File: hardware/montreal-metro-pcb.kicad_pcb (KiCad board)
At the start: 2 copper layers, 160 x 160 mm, 95 parts, among them SW1 TS-1187A-B-A-B, SW2 TS-1187A-B-A-B, SW3 TS-1187A-B-A-B, SW4 TS-1187A-B-A-B, U1 XIAO-RP2040-DIP

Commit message: Official names, hand-pass label defaults, and an unrouted board
- labels: restore the official hyphenated names in the six hand-typed
  labels, keeping the hand-chosen line breaks
- auto_label: defaults now follow the hand pass - beside the station and
  level with it, right before left, nudged only as far as needed, one side
  per run, above / below alternating on level runs, leaders last
- board: every track and via removed; routing will be done by hand.
  Artwork regenerated from the frozen labels (water cut back under them)
- rebuild_board.sh no longer routes unless given --autoroute;
  autoroute.py gains "clear"

DRC: no violations, 0 schematic parity issues, 167 unconnected items
(nothing is routed).

Co-Authored-By: Claude Opus 5.5 <noreply@anthropic.com>
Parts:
- moved ROW5 6.00 mm to (83.2, 81.3)
- moved ROW1 4.24 mm to (140.8, 19.2), turned to 90 degrees
- moved ROW3 2.97 mm to (20.2, 74.7), turned to 0 degrees
- moved ROW2 1.39 mm to (62.2, 47.4), turned to 0 degrees
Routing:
- net +5V: track 740.2 -> 0.00 mm, vias 21 -> 0
- net GND: track 262.2 -> 0.00 mm, vias 32 -> 0
- net LED_OUT: track 97.1 -> 0.00 mm, vias 3 -> 0
- net LED_IN: track 73.3 -> 0.00 mm, vias 1 -> 0
- net Net-(LED64-DO): track 55.1 -> 0.00 mm, vias 2 -> 0
- net Net-(LED31-DO): track 53.3 -> 0.00 mm, vias 2 -> 0
- net BUTTON_02: track 38.9 -> 0.00 mm, vias 2 -> 0
- net BUTTON_04: track 28.8 -> 0.00 mm, vias 2 -> 0
- net Net-(LED15-DO): track 27.2 -> 0.00 mm, vias 2 -> 0
- net BUTTON_01: track 26.1 -> 0.00 mm, vias 2 -> 0
- net Net-(LED2-DO): track 24.1 -> 0.00 mm, vias 2 -> 0
- net ROW6: track 19.1 -> 0.00 mm, vias 2 -> 0
- net BUTTON_03: track 16.6 -> 0.00 mm
- net Net-(LED1-DO): track 13.5 -> 0.00 mm, vias 2 -> 0
- net Net-(LED67-DO): track 12.5 -> 0.00 mm, vias 2 -> 0
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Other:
- board text added: "Champ-de- Mars"
- board text added: "Henri-Bourassa"
- board text added: "Honoré-Beaugrand"
- board text added: "Jean-Talon"
- board text added: "Lucien-L'Allier"
- board text added: "Mont-Royal"
- board text added: "Place- d'Armes"
- board text removed: "Champ-de Mars"
- board text removed: "Henri Bourassa"
- board text removed: "Honoré Beaugrand"
- board text removed: "Jean Talon"
- board text removed: "Lucien L'Allier"
- board text removed: "Mont Royal"
- board text removed: "Place d'Armes"

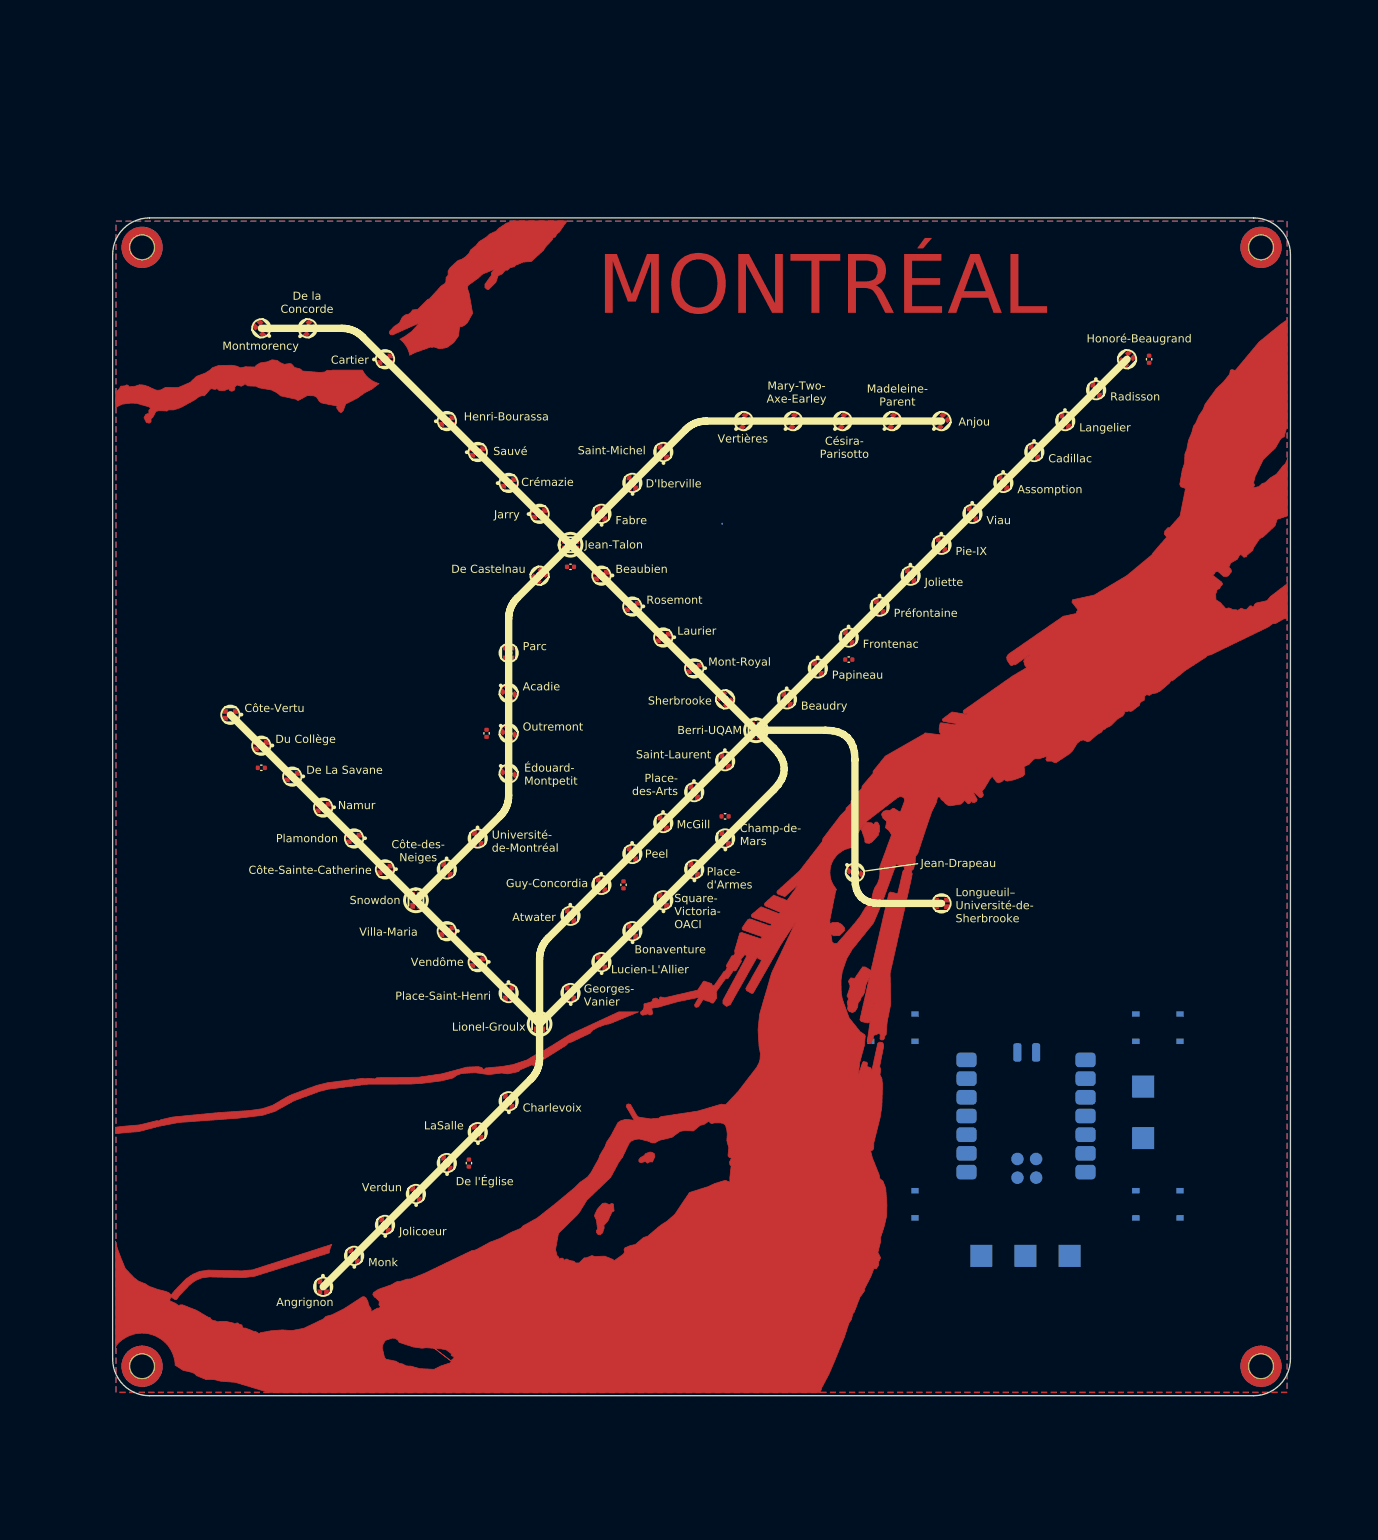
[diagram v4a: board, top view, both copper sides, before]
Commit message: Hand-routed board, R1 and C1, owl back art, JLCPCB outputs
The board is now routed by hand with every assembled part on the
top side. Added:

- C1, 100 uF 6.3 V 1206 X5R bulk capacitor (LCSC C15008, basic)
  on the +5V trunk.
- R1, 330 R 0402 (LCSC C25104, basic) in series on the LED data
  line. U1 pin 8 and the LED_IN1 test point are now on LED_DATA;
  LED_IN runs from R1 to LED1 only.
- The snowy-owl artwork on the back silkscreen as the board-only
  footprint LOGO1, generated by the new tools/svg_to_silk.py.
- JLCPCB gerbers, BOM and CPL in hardware/jlcpcb, stamped
  2026-10-18-1117; make_jlcpcb.py takes the stamp as an argument.
- The latest hand label edits, imported and frozen.

DRC: no errors, 0 unconnected, 0 schematic parity issues.

Co-Authored-By: Claude Opus 5.5 <noreply@anthropic.com>
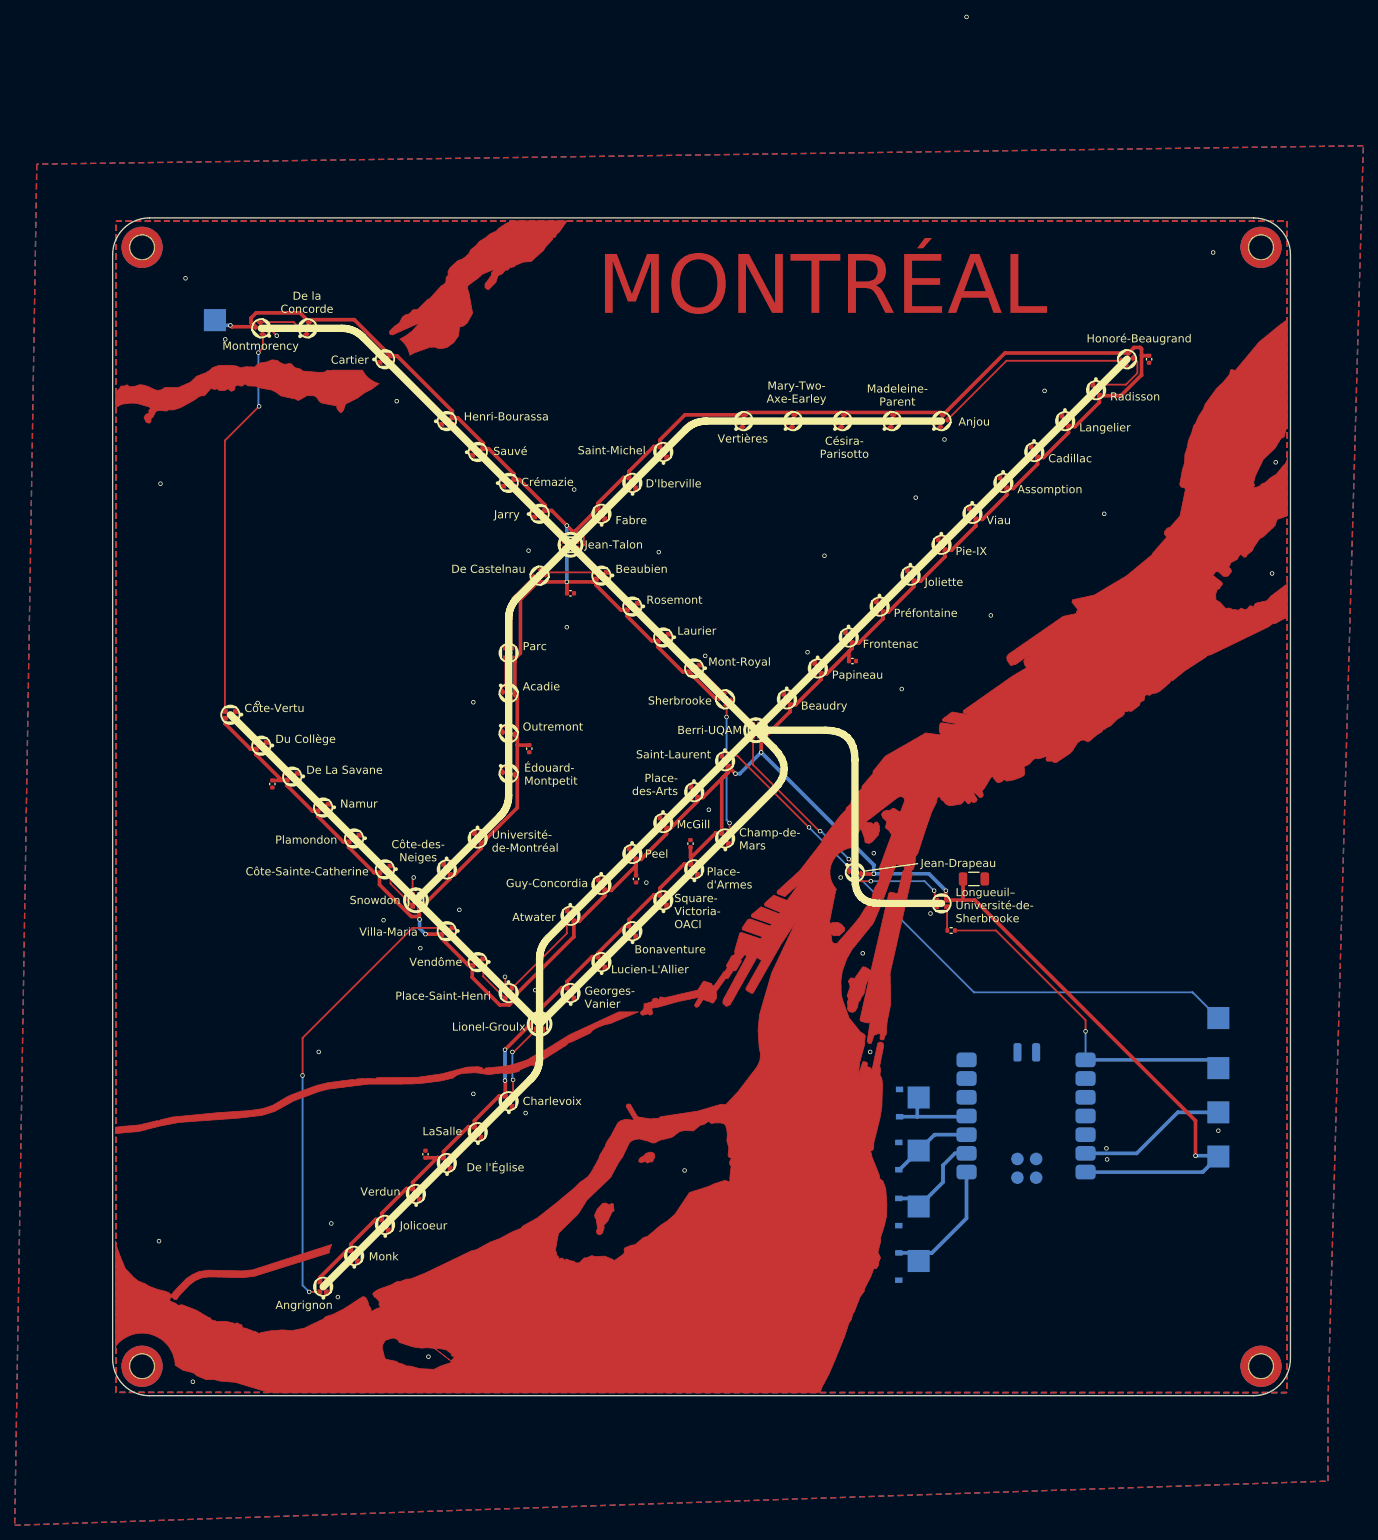
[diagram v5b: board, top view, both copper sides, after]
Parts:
- added C1: 100uF,6.3V,X5R, Capacitor_SMD:C_1206_3216Metric, F.Cu at (117.0, 89.8)
- added LOGO1: artwork, , B.Cu at (80.0, 54.5)
- added R1: 330R, Resistor_SMD:R_0402_1005Metric, F.Cu at (113.9, 96.8)
- added TP1: TestPoint, TestPoint:TestPoint_Pad_3.0x3.0mm, B.Cu at (109.5, 141.7)
- added TP2: TestPoint, TestPoint:TestPoint_Pad_3.0x3.0mm, B.Cu at (109.5, 134.3)
- added TP3: TestPoint, TestPoint:TestPoint_Pad_3.0x3.0mm, B.Cu at (109.5, 126.7)
- added TP4: TestPoint, TestPoint:TestPoint_Pad_3.0x3.0mm, B.Cu at (109.5, 119.5)
- moved +5V1 163.5 mm to (13.9, 13.9), turned to 180 degrees
- moved SW2 42.0 mm to (103.8, 127.5), turned to 0 degrees
- moved LED_IN1 41.1 mm to (150.2, 115.5), turned to -90 degrees
- moved SW4 40.5 mm to (103.9, 120.2), turned to 0 degrees
- moved GND1 32.7 mm to (150.2, 121.5), turned to -90 degrees
- moved SW1 32.5 mm to (103.8, 142.4)
- moved +5V2 24.3 mm to (150.2, 127.5), turned to -90 degrees
- moved LED_OUT1 19.2 mm to (150.2, 108.7)
- moved ROW4 6.16 mm to (56.6, 72.1)
- moved ROW6 6.02 mm to (42.5, 127.2), turned to -90 degrees
- moved ROW5 5.98 mm to (78.5, 85.0), turned to -90 degrees
- moved ROW2 3.60 mm to (62.2, 51.0), turned to 180 degrees
- moved ROW3 2.66 mm to (21.7, 76.9), turned to 90 degrees
- moved SW3 2.44 mm to (103.8, 135.1)
- moved ROW7 1.88 mm to (71.1, 89.8)
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- renumbered SW3 to SW2, SW2 to SW3
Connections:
- LED_IN1 pad 1: LED_IN -> LED_DATA
- SW2 pad 1: BUTTON_02 -> unconnected-(SW2-A-Pad1)
- SW2 pad 2: unconnected-(SW3-B-Pad2) -> BUTTON_03
- SW3 pad 1: unconnected-(SW2-A-Pad1) -> BUTTON_02
- SW3 pad 2: BUTTON_03 -> unconnected-(SW3-B-Pad2)
- U1 pad 8: LED_IN -> LED_DATA
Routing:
- net +5V: track 0.00 -> 678.2 mm, vias 0 -> 12
- net LED_OUT: track 0.00 -> 81.3 mm, vias 0 -> 1
- net Net-(LED64-DO): track 0.00 -> 61.4 mm, vias 0 -> 2
- net Net-(LED31-DO): track 0.00 -> 53.4 mm, vias 0 -> 2
- net LED_DATA: track 0.00 -> 46.7 mm, vias 0 -> 1
- net Net-(LED15-DO): track 0.00 -> 26.8 mm
- net GND: track 0.00 -> 25.8 mm, vias 0 -> 49
- net Net-(LED2-DO): track 0.00 -> 23.5 mm, vias 0 -> 2
- net ROW6: track 0.00 -> 17.5 mm, vias 0 -> 2
- net BUTTON_01: track 0.00 -> 17.4 mm
- net Net-(LED1-DO): track 0.00 -> 12.6 mm, vias 0 -> 2
- net BUTTON_02: track 0.00 -> 12.3 mm
- net Net-(LED67-DO): track 0.00 -> 12.2 mm
- net BUTTON_04: track 0.00 -> 11.7 mm
- net ROW3: track 0.00 -> 11.1 mm
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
